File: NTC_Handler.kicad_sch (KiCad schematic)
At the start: 48 parts

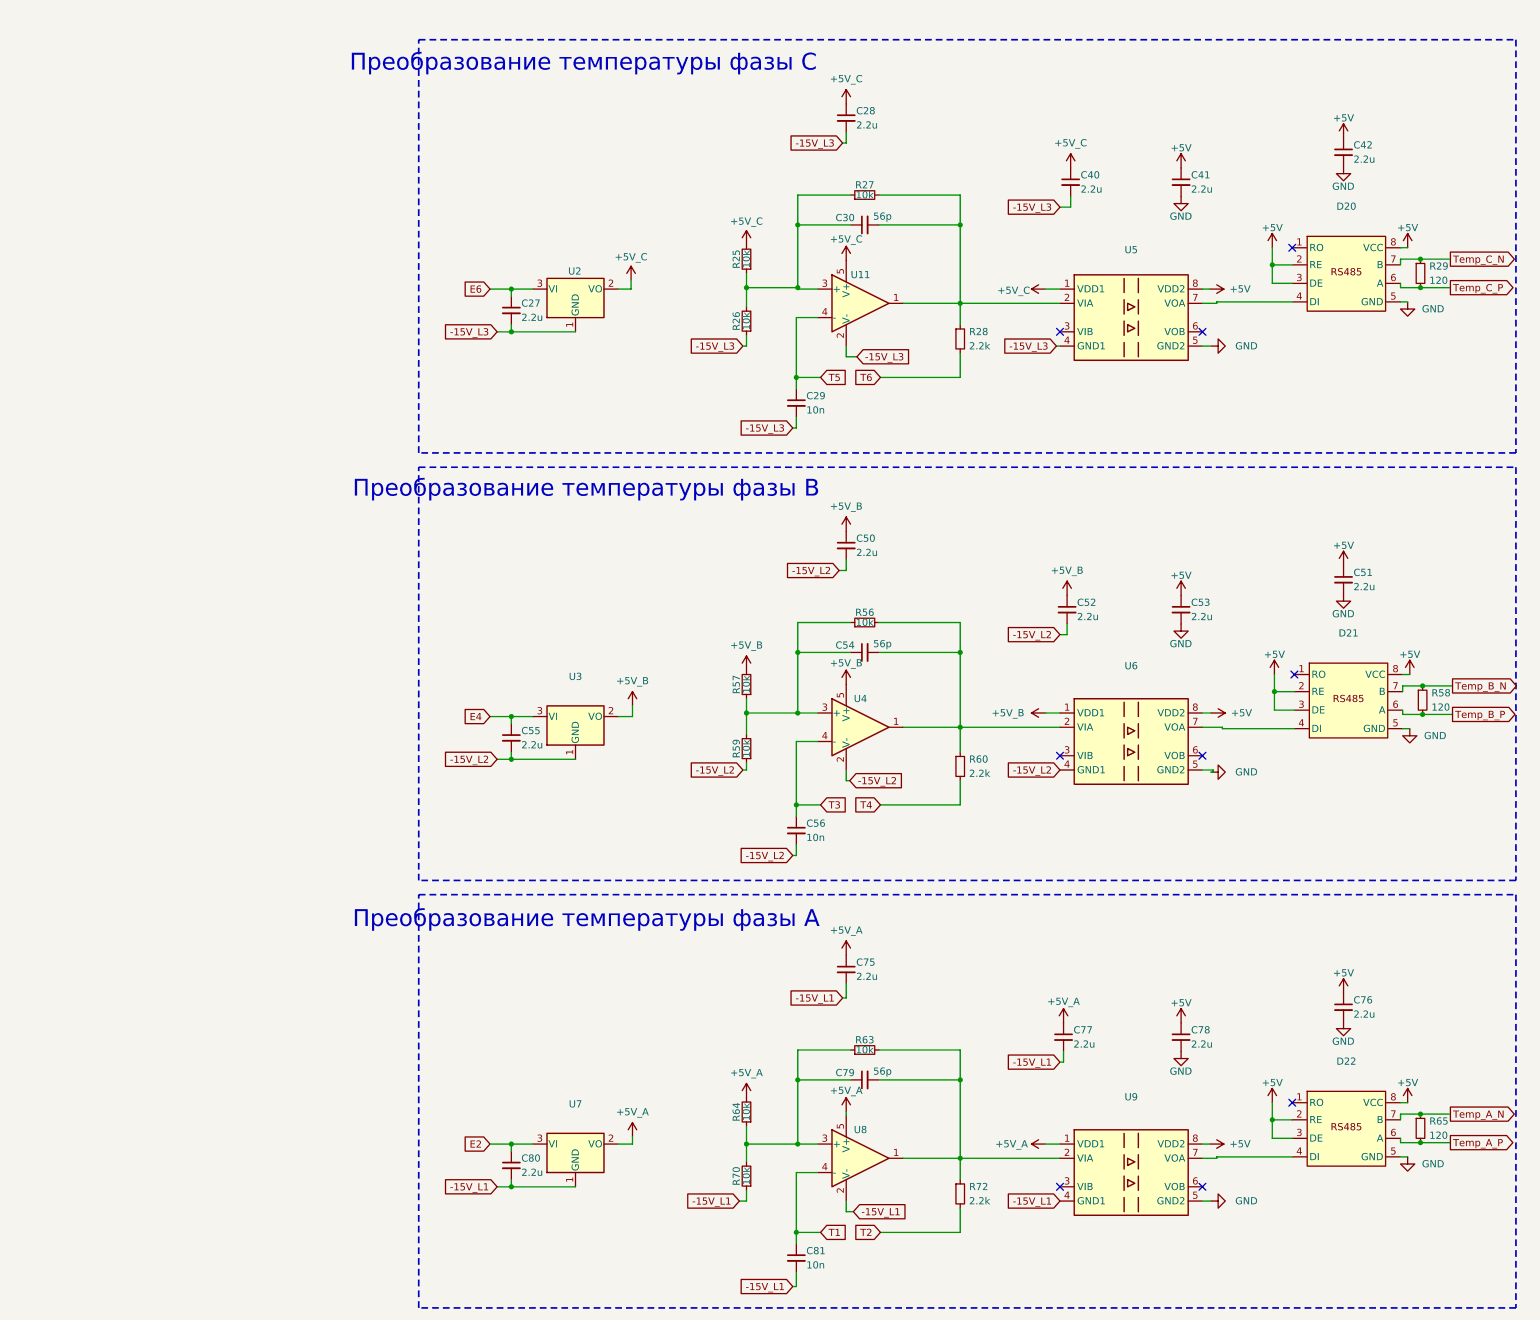
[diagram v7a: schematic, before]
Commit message: VER2.2: сделал изоллированное питание для температурных контуров
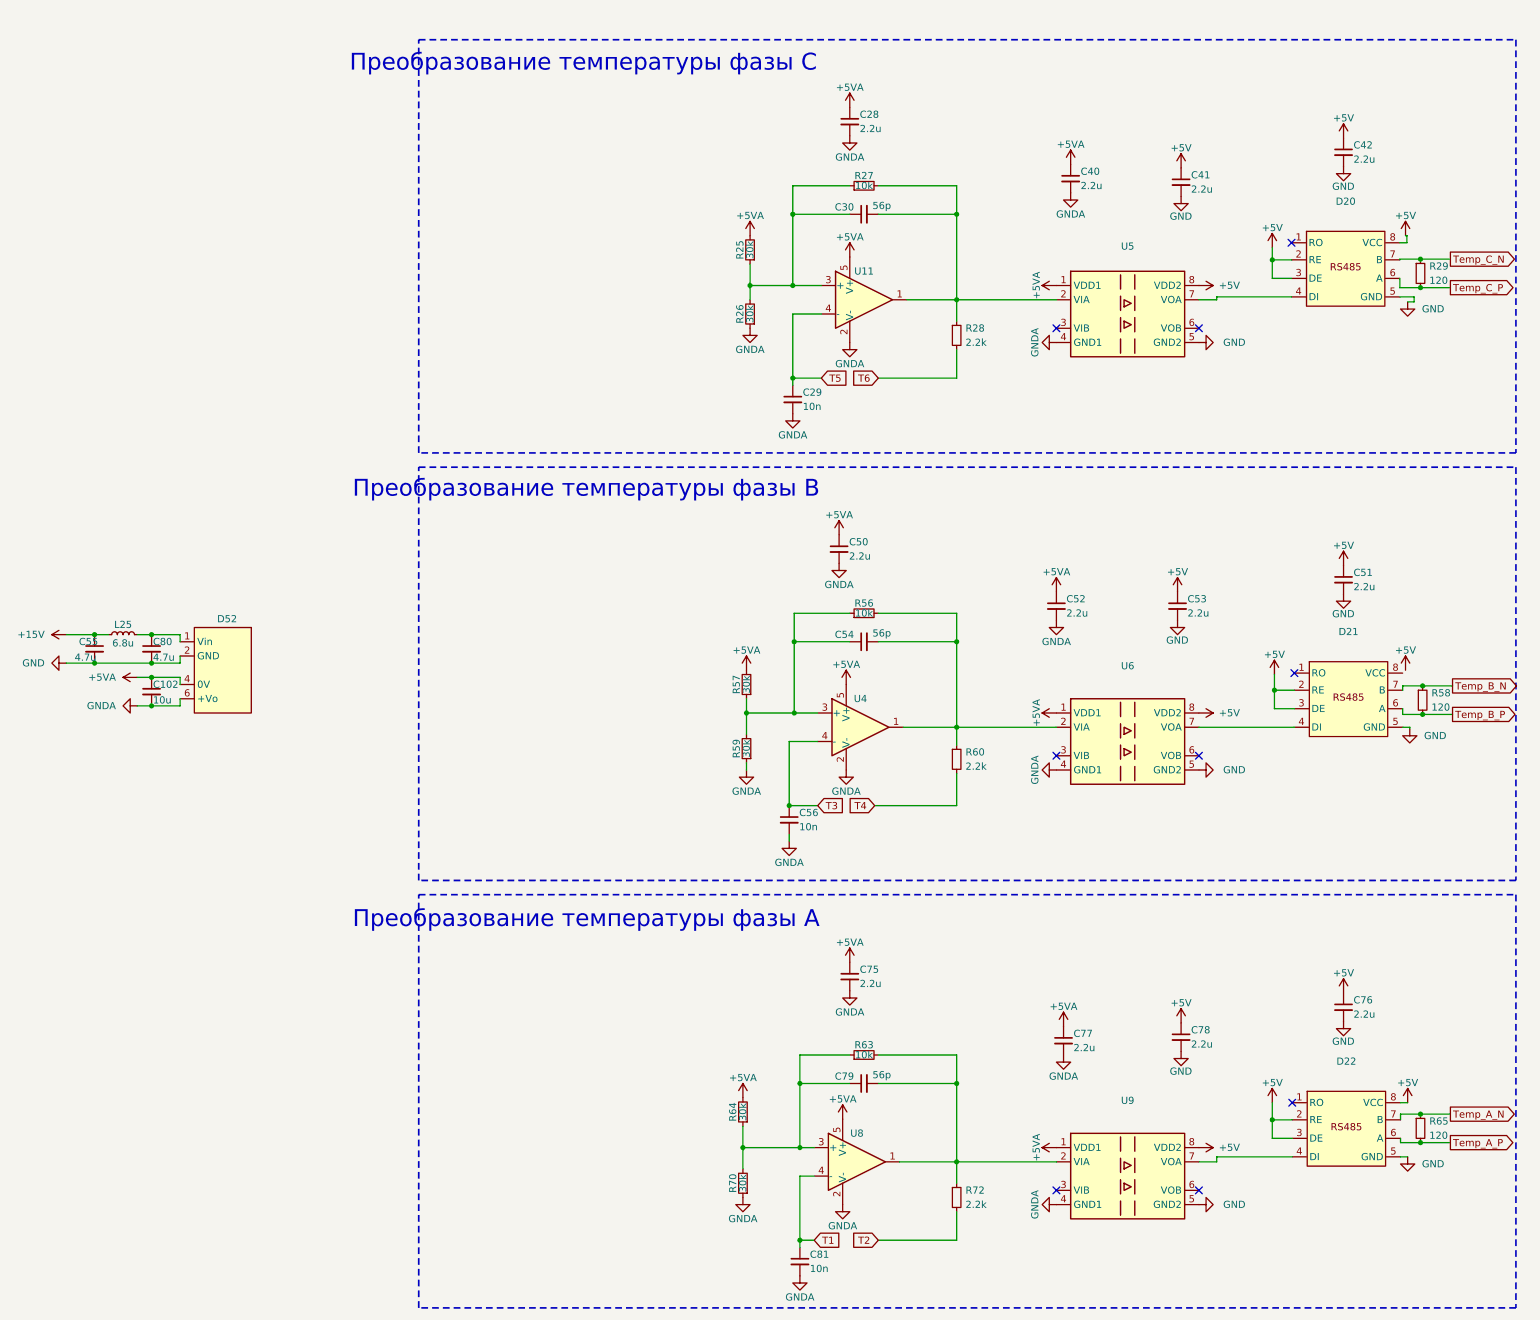
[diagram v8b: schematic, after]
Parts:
- removed C27: 2.2u, Capacitor_SMD:C_0805_2012Metric_Pad1.18x1.45mm_HandSolder, symbol Device:C_Small
- removed U2, U3, U7: ~, Package_TO_SOT_SMD:SOT-223, symbol Regulator_Linear:LM1117-3.3
- added C102: 10u, Capacitor_SMD:C_1206_3216Metric_Pad1.33x1.80mm_HandSolder, symbol Device:C_Small
- added D52: ~, Mornsun_my:B_LS-1WR3, symbol Mornsun_my:A_XT-1WR3
- added L25: 6.8u, Inductor_SMD:L_0805_2012Metric_Pad1.15x1.40mm_HandSolder, symbol Device:L_Small
- C55, C80: value 2.2u -> 4.7u; footprint Capacitor_SMD:C_0805_2012Metric_Pad1.18x1.45mm_HandSolder -> Capacitor_SMD:C_1206_3216Metric_Pad1.33x1.80mm_HandSolder
- R25, R26, R57, R59, R64, R70: value 10k -> 30k
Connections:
- net +5V_B is gone; now on net +5VA: C50.1, C52.1, R57.2, U4.5 (V+), U6.1 (VDD1)
- net +5V_C is gone; now on net +5VA: C28.1, C40.1, R25.2, U11.5 (V+), U5.1 (VDD1)
- net -15V_L3 is gone; now on net GNDA: C28.2, C29.2, C40.2, R26.1, U11.2 (V-), U5.4 (GND1)
- net +5V: no longer D21.8 (VCC)
- net GND: now also C55.2, C80.2, D52.2 (GND)
- net +5V_A renamed +5VA
- net +5VA: now also C102.1, D52.4 (0V)
- net -15V_L1 renamed GNDA
- net GNDA: now also C50.2, C52.2, C56.2, R59.1, U4.2 (V-), U6.4 (GND1), C102.2, D52.6 (+Vo); no longer C80.2
- removed net -15V_L2: C50.2, C52.2, C55.2, C56.2, R59.1, U4.2 (V-), U6.4 (GND1)
- net E2: no longer names the net of C80.1
- net E2: now also D52.1 (Vin), L25.2
- net E4 renamed +15V
- net +15V: now also L25.1
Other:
- moved on the sheet: C28, C29, C30, C40, C50, C52, C53, C54, C56, C75, C77, C79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
